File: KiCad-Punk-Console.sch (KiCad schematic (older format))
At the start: 16 parts, among them U1 NE556

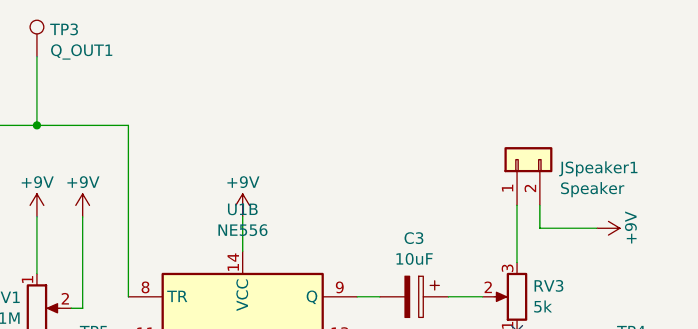
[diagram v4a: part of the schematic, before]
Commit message: added fiducial markers for automated placements of parts
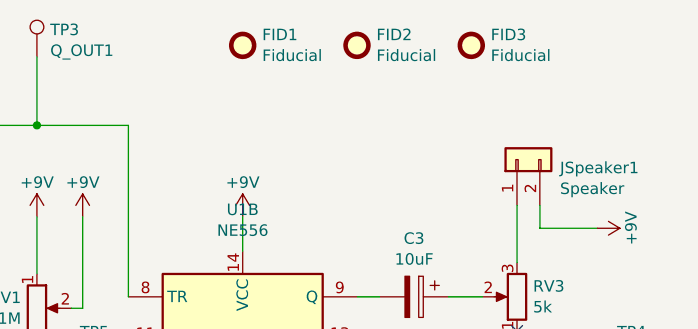
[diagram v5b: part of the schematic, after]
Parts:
- added FID1, FID2, FID3: Fiducial, symbol Mechanical:Fiducial
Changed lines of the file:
@@
 Wire Wire Line
 	5300 3500 5800 3500
+$Comp
+L Mechanical:Fiducial FID1
+U 1 1 5D884543
+P 6700 2200
+F 0 "FID1" H 6785 2246 50  0000 L CNN
+F 1 "Fiducial" H 6785 2155 50  0000 L CNN
+F 2 "" H 6700 2200 50  0001 C CNN
+F 3 "~" H 6700 2200 50  0001 C CNN
+	1    6700 2200
+	1    0    0    -1
+$EndComp
+$Comp
+L Mechanical:Fiducial FID2
+U 1 1 5D8849CD
+P 7200 2200
+F 0 "FID2" H 7285 2246 50  0000 L CNN
+F 1 "Fiducial" H 7285 2155 50  0000 L CNN
+F 2 "" H 7200 2200 50  0001 C CNN
+F 3 "~" H 7200 2200 50  0001 C CNN
+	1    7200 2200
+	1    0    0    -1
+$EndComp
+$Comp
+L Mechanical:Fiducial FID3
+U 1 1 5D884D25
+P 7700 2200
+F 0 "FID3" H 7785 2246 50  0000 L CNN
+F 1 "Fiducial" H 7785 2155 50  0000 L CNN
+F 2 "" H 7700 2200 50  0001 C CNN
+F 3 "~" H 7700 2200 50  0001 C CNN
+	1    7700 2200
+	1    0    0    -1
+$EndComp
 $EndSCHEMATC

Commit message: added parts
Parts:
- BT9V1: footprint (none) -> Battery:BatteryHolder_Eagle_12BH611-GR
- C1: footprint (none) -> Capacitor_THT:CP_Radial_D5.0mm_P2.00mm
- C2: footprint (none) -> Capacitor_THT:C_Axial_L3.8mm_D2.6mm_P7.50mm_Horizontal
- C3: footprint (none) -> Capacitor_THT:CP_Axial_L11.0mm_D8.0mm_P15.00mm_Horizontal
- FID1, FID2, FID3: footprint (none) -> Fiducial:Fiducial_1mm_Mask3mm
- JSpeaker1: footprint (none) -> Connector_Wire:SolderWirePad_1x02_P3.81mm_Drill1.2mm
- R1: footprint (none) -> Resistor_THT:R_Axial_DIN0204_L3.6mm_D1.6mm_P5.08mm_Horizontal
- RV1, RV2, RV3: footprint (none) -> Potentiometer_THT:Potentiometer_Bourns_PTV09A-1_Single_Vertical
- SWOnOff1: footprint (none) -> Button_Switch_SMD:SW_SPDT_CK-JS102011SAQN
- TP1, TP2, TP3, TP4, TP5: footprint (none) -> TestPoint:TestPoint_Keystone_5005-5009_Compact
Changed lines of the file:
@@
 F 0 "RV1" H 5731 3396 50  0000 R CNN
 F 1 "1M" H 5731 3305 50  0000 R CNN
-F 2 "" H 5800 3350 50  0001 C CNN
+F 2 "Potentiometer_THT:Potentiometer_Bourns_PTV09A-1_Single_Vertical" H 5800 3350 50  0001 C CNN
 F 3 "~" H 5800 3350 50  0001 C CNN
 	1    5800 3350
@@
 F 0 "RV3" H 7830 3254 50  0000 R CNN
 F 1 "5k" H 7830 3345 50  0000 R CNN
-F 2 "" H 7900 3300 50  0001 C CNN
+F 2 "Potentiometer_THT:Potentiometer_Bourns_PTV09A-1_Single_Vertical" H 7900 3300 50  0001 C CNN
 F 3 "~" H 7900 3300 50  0001 C CNN
 	1    7900 3300
@@
 F 0 "RV2" V 7450 3950 50  0000 C CNN
 F 1 "1M" V 7334 3700 50  0000 C CNN
-F 2 "" H 7450 3700 50  0001 C CNN
+F 2 "Potentiometer_THT:Potentiometer_Bourns_PTV09A-1_Single_Vertical" H 7450 3700 50  0001 C CNN
 F 3 "~" H 7450 3700 50  0001 C CNN
 	1    7450 3700
@@
 F 0 "R1" H 5870 3796 50  0000 L CNN
 F 1 "1k" H 5870 3705 50  0000 L CNN
-F 2 "" V 5730 3750 50  0001 C CNN
+F 2 "Resistor_THT:R_Axial_DIN0204_L3.6mm_D1.6mm_P5.08mm_Horizontal" V 5730 3750 50  0001 C CNN
 F 3 "~" H 5800 3750 50  0001 C CNN
 	1    5800 3750
@@
 F 0 "C2" H 7315 3996 50  0000 L CNN
 F 1 "100nF" H 7315 3905 50  0000 L CNN
-F 2 "" H 7238 3800 50  0001 C CNN
+F 2 "Capacitor_THT:C_Axial_L3.8mm_D2.6mm_P7.50mm_Horizontal" H 7238 3800 50  0001 C CNN
 F 3 "~" H 7200 3950 50  0001 C CNN
 	1    7200 3950
@@
 F 0 "C1" H 4515 4146 50  0000 L CNN
 F 1 "10nF" H 4515 4055 50  0000 L CNN
-F 2 "" H 4438 3950 50  0001 C CNN
+F 2 "Capacitor_THT:CP_Radial_D5.0mm_P2.00mm" H 4438 3950 50  0001 C CNN
 F 3 "~" H 4400 4100 50  0001 C CNN
 	1    4400 4100
@@
 F 0 "C3" V 7195 3300 50  0000 C CNN
 F 1 "10uF" V 7286 3300 50  0000 C CNN
-F 2 "" H 7488 3150 50  0001 C CNN
+F 2 "Capacitor_THT:CP_Axial_L11.0mm_D8.0mm_P15.00mm_Horizontal" H 7488 3150 50  0001 C CNN
 F 3 "~" H 7450 3300 50  0001 C CNN
 	1    7450 3300
@@
 F 0 "BT9V1" H 3568 3896 50  0000 L CNN
 F 1 "9V" H 3568 3805 50  0000 L CNN
-F 2 "" V 3450 3860 50  0001 C CNN
+F 2 "Battery:BatteryHolder_Eagle_12BH611-GR" V 3450 3860 50  0001 C CNN
 F 3 "~" V 3450 3860 50  0001 C CNN
 	1    3450 3800
@@
 F 0 "JSpeaker1" V 7864 2512 50  0000 R CNN
 F 1 "Speaker" V 7773 2512 50  0000 R CNN
-F 2 "" H 7900 2700 50  0001 C CNN
+F 2 "Connector_Wire:SolderWirePad_1x02_P3.81mm_Drill1.2mm" H 7900 2700 50  0001 C CNN
 F 3 "~" H 7900 2700 50  0001 C CNN
 	1    7900 2700
@@
 F 0 "SWOnOff1" V 3496 3112 50  0000 R CNN
 F 1 "SW_SPDT" V 3405 3112 50  0000 R CNN
-F 2 "" H 3450 3300 50  0001 C CNN
+F 2 "Button_Switch_SMD:SW_SPDT_CK-JS102011SAQN" H 3450 3300 50  0001 C CNN
 F 3 "~" H 3450 3300 50  0001 C CNN
 	1    3450 3300
@@
 F 0 "TP1" V 3454 3188 50  0000 L CNN
 F 1 "9V" V 3545 3188 50  0000 L CNN
-F 2 "" H 3700 3000 50  0001 C CNN
+F 2 "TestPoint:TestPoint_Keystone_5005-5009_Compact" H 3700 3000 50  0001 C CNN
 F 3 "~" H 3700 3000 50  0001 C CNN
 	1    3500 3000
@@
 F 0 "TP2" V 3454 4138 50  0000 L CNN
 F 1 "GND" V 3545 4138 50  0000 L CNN
-F 2 "" H 3700 3950 50  0001 C CNN
+F 2 "TestPoint:TestPoint_Keystone_5005-5009_Compact" H 3700 3950 50  0001 C CNN
 F 3 "~" H 3700 3950 50  0001 C CNN
 	1    3500 3950
@@
 F 0 "TP4" V 8104 3688 50  0000 L CNN
 F 1 "POT12" V 8195 3688 50  0000 L CNN
-F 2 "" H 8350 3500 50  0001 C CNN
+F 2 "TestPoint:TestPoint_Keystone_5005-5009_Compact" H 8350 3500 50  0001 C CNN
 F 3 "~" H 8350 3500 50  0001 C CNN
 	1    8150 3500
@@
 F 0 "TP3" H 5858 2368 50  0000 L CNN
 F 1 "Q_OUT1" H 5858 2277 50  0000 L CNN
-F 2 "" H 6000 2250 50  0001 C CNN
+F 2 "TestPoint:TestPoint_Keystone_5005-5009_Compact" H 6000 2250 50  0001 C CNN
 F 3 "~" H 6000 2250 50  0001 C CNN
 	1    5800 2250
@@
 F 0 "TP5" V 5754 3688 50  0000 L CNN
 F 1 "POT1" V 5845 3688 50  0000 L CNN
-F 2 "" H 6000 3500 50  0001 C CNN
+F 2 "TestPoint:TestPoint_Keystone_5005-5009_Compact" H 6000 3500 50  0001 C CNN
 F 3 "~" H 6000 3500 50  0001 C CNN
 	1    5800 3500
@@
 F 0 "FID1" H 6785 2246 50  0000 L CNN
 F 1 "Fiducial" H 6785 2155 50  0000 L CNN
-F 2 "" H 6700 2200 50  0001 C CNN
+F 2 "Fiducial:Fiducial_1mm_Mask3mm" H 6700 2200 50  0001 C CNN
 F 3 "~" H 6700 2200 50  0001 C CNN
 	1    6700 2200
@@
 F 0 "FID2" H 7285 2246 50  0000 L CNN
 F 1 "Fiducial" H 7285 2155 50  0000 L CNN
-F 2 "" H 7200 2200 50  0001 C CNN
+F 2 "Fiducial:Fiducial_1mm_Mask3mm" H 7200 2200 50  0001 C CNN
 F 3 "~" H 7200 2200 50  0001 C CNN
 	1    7200 2200
@@
 F 0 "FID3" H 7785 2246 50  0000 L CNN
 F 1 "Fiducial" H 7785 2155 50  0000 L CNN
-F 2 "" H 7700 2200 50  0001 C CNN
+F 2 "Fiducial:Fiducial_1mm_Mask3mm" H 7700 2200 50  0001 C CNN
 F 3 "~" H 7700 2200 50  0001 C CNN
 	1    7700 2200
